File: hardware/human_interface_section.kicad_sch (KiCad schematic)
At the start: 8 parts, among them J1 Conn_01x08, J2 Micro_SD_Card, SW1 SW_Push, SW2 SW_Push, SW3 SW_Push, SW4 SW_Push, SW5 SW_Push, SW6 SW_Push

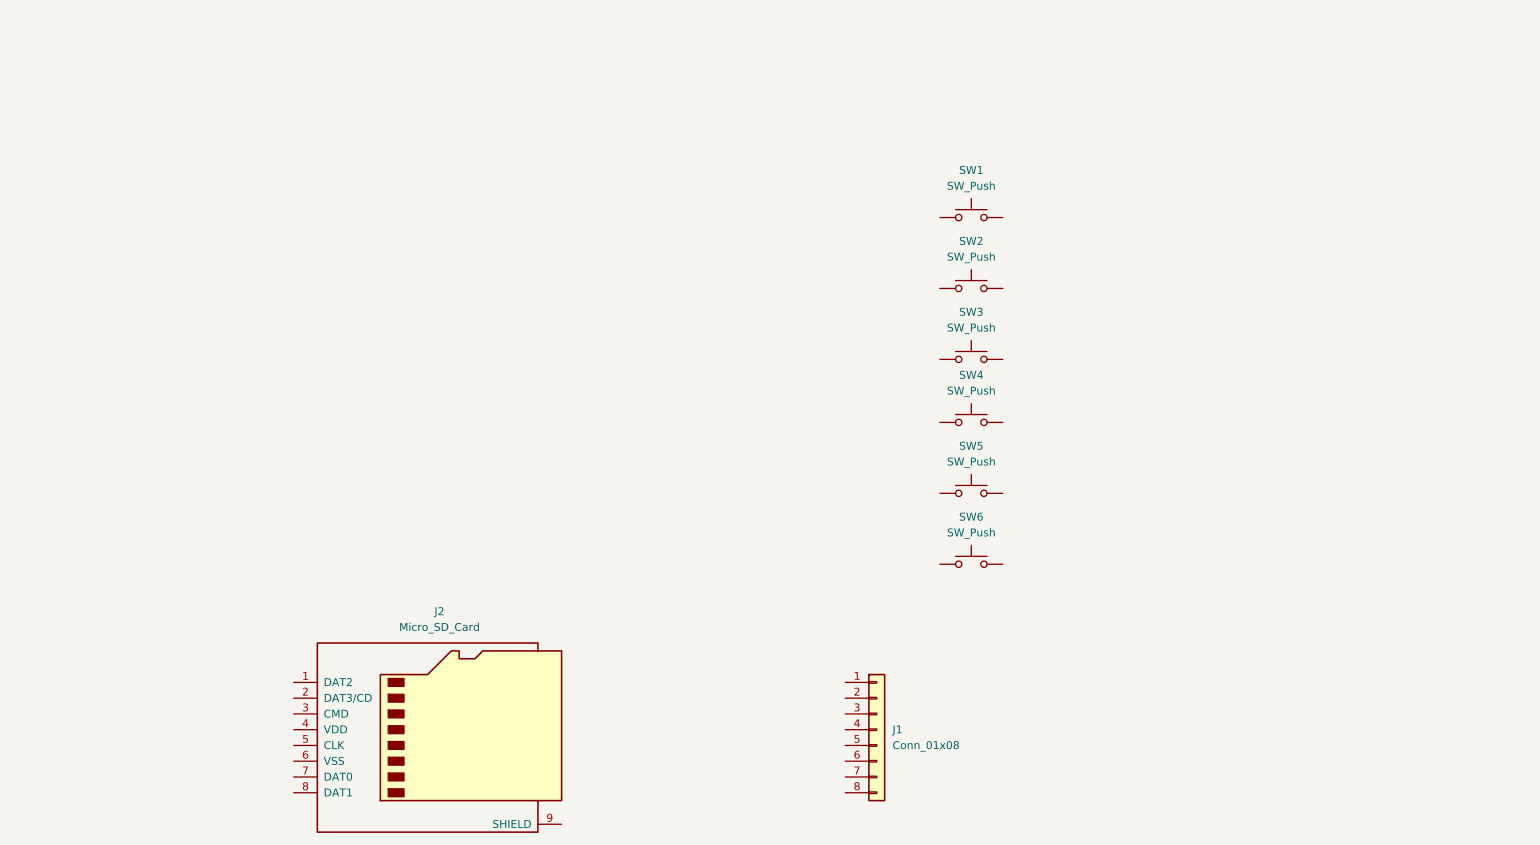
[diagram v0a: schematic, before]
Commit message: Human Interface section finished
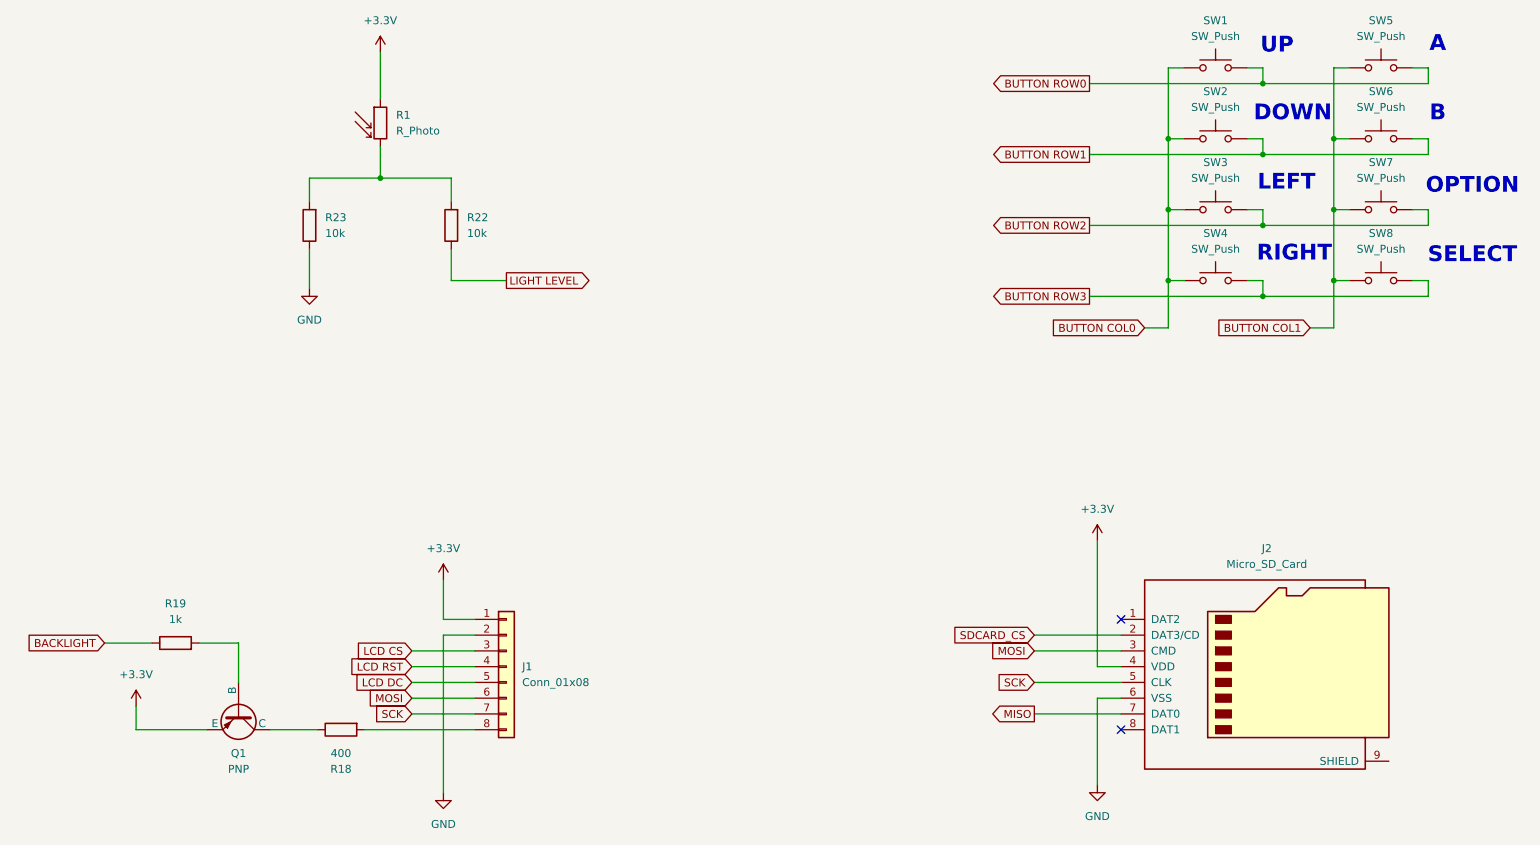
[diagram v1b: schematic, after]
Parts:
- added Q1: PNP, symbol Simulation_SPICE:PNP
- added R1: R_Photo, symbol Device:R_Photo
- added R18: 400, Resistor_SMD:R_0603_1608Metric, symbol Device:R
- added R19: 1k, Resistor_SMD:R_0603_1608Metric, symbol Device:R
- added R22, R23: 10k, Resistor_SMD:R_0603_1608Metric, symbol Device:R
- added SW7, SW8: SW_Push, symbol Switch:SW_Push
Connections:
- net BUTTON COL0: now reaches SW2.1
- net BUTTON COL0: now also SW1.1, SW3.1, SW4.1
- net BUTTON ROW1: now reaches SW2.2
- net BUTTON ROW1: now also SW6.2
- net BUTTON COL1: now reaches SW6.1
- net BUTTON COL1: now also SW5.1, SW7.1, SW8.1
- net BUTTON ROW2: now reaches SW3.2
- net BUTTON ROW2: now also SW7.2
- net BUTTON ROW0: now reaches SW1.2
- net BUTTON ROW0: now also SW5.2
- net BUTTON ROW3: now reaches SW4.2
- net BUTTON ROW3: now also SW8.2
- net SDCARD_CS: now reaches J2.2 (DAT3/CD)
- net MOSI: now reaches J2.3 (CMD)
- net MOSI: now also J1.6 (Pin_6)
- net +3.3V: now reaches J2.4 (VDD)
- net +3.3V: now also J1.1 (Pin_1), Q1.3 (E), R1.1
- net SCK: now reaches J2.5 (CLK)
- net SCK: now also J1.7 (Pin_7)
- net GND: now reaches J2.6 (VSS)
- net GND: now also J1.2 (Pin_2), R23.1
- net MISO: now reaches J2.7 (DAT0)
- net LCD CS: now reaches J1.3 (Pin_3)
- net LCD RST: now reaches J1.4 (Pin_4)
- net LCD DC: now reaches J1.5 (Pin_5)
- net at J1.8 (Pin_8): now also R18.2
- new net: Q1.2 (B), R19.2
- new net: R1.2, R22.2, R23.2
- new net: Q1.1 (C), R18.1
- new net BACKLIGHT: R19.1
- new net LIGHT LEVEL: R22.1
- no-connect marks 0 -> 2
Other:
- note added: "A"
- note added: "B"
- note added: "DOWN"
- note added: "LEFT"
- note added: "OPTION"
- note added: "RIGHT"
- note added: "SELECT"
- note added: "UP"
- moved on the sheet: J1, J2, SW1, SW2, SW3, SW4

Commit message: Moved MCU to general section
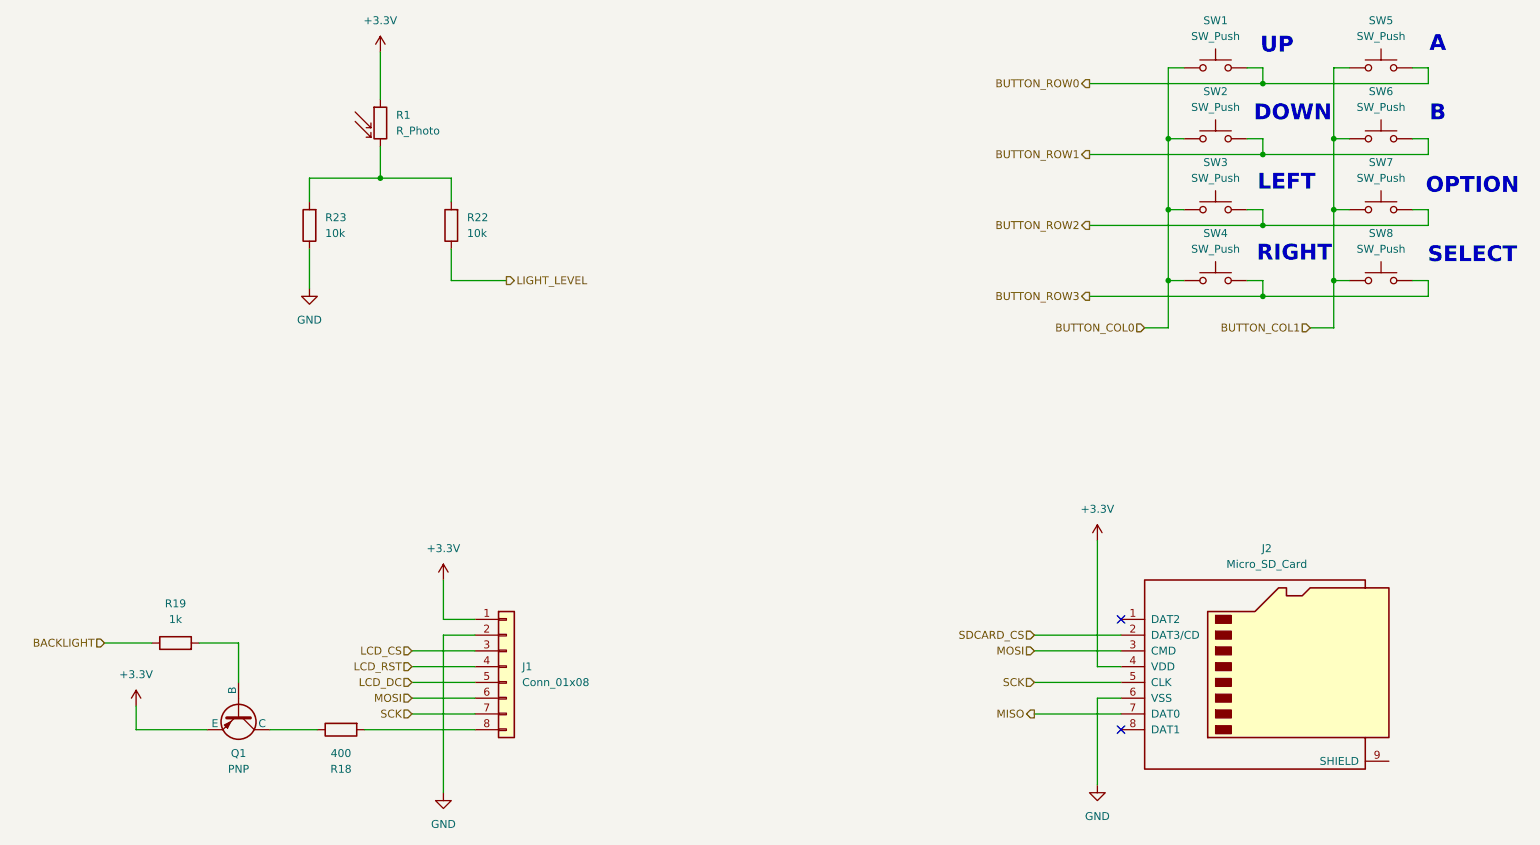
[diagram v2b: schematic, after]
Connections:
- net BUTTON COL0 renamed BUTTON_COL0
- net BUTTON COL1 renamed BUTTON_COL1
- net BUTTON ROW0 renamed BUTTON_ROW0
- net BUTTON ROW1 renamed BUTTON_ROW1
- net BUTTON ROW2 renamed BUTTON_ROW2
- net BUTTON ROW3 renamed BUTTON_ROW3
- net LCD CS renamed LCD_CS
- net LCD DC renamed LCD_DC
- net LCD RST renamed LCD_RST
- net LIGHT LEVEL renamed LIGHT_LEVEL
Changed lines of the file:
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@@
 		)
 	)
-	(global_label "BUTTON ROW3"
-		(shape output)
-		(at 194.31 73.66 180)
-		(fields_autoplaced yes)
+	(hierarchical_label "BACKLIGHT"
+		(shape input)
+		(at 35.56 129.54 180)
 		(effects
 			(font
@@
 			(justify right)
 		)
-		(property "Intersheetrefs" "${INTERSHEET_REFS}"
-			(at 177.8991 73.66 0)
-			(effects
-				(font
-					(size 1.27 1.27)
-				)
-				(justify right)
-				(hide yes)
-			)
-		)
 	)
-	(global_label "BUTTON ROW1"
-		(shape output)
-		(at 194.31 50.8 180)
-		(fields_autoplaced yes)
+	(hierarchical_label "LCD_DC"
+		(shape input)
+		(at 85.09 135.89 180)
 		(effects
 			(font
@@
 			(justify right)
 		)
-		(property "Intersheetrefs" "${INTERSHEET_REFS}"
-			(at 177.8991 50.8 0)
-			(effects
-				(font
-					(size 1.27 1.27)
-				)
-				(justify right)
-				(hide yes)
+	)
+	(hierarchical_label "LIGHT_LEVEL"
+		(shape output)
+		(at 100.33 71.12 0)
+		(effects
+			(font
+				(size 1.27 1.27)
 			)
+			(justify left)
 		)
 	)
-	(global_label "SCK"
-		(shape input)
-		(at 85.09 140.97 180)
-		(fields_autoplaced yes)
+	(hierarchical_label "BUTTON_ROW3"
+		(shape output)
+		(at 194.31 73.66 180)
 		(effects
 			(font
@@
 			(justify right)
 		)
-		(property "Intersheetrefs" "${INTERSHEET_REFS}"
-			(at 78.3553 140.97 0)
-			(effects
-				(font
-					(size 1.27 1.27)
-				)
-				(justify right)
-				(hide yes)
-			)
-		)
 	)
-	(global_label "BACKLIGHT"
+	(hierarchical_label "MOSI"
 		(shape input)
-		(at 35.56 129.54 180)
-		(fields_autoplaced yes)
+		(at 185.42 130.81 180)
 		(effects
 			(font
@@
 			(justify right)
 		)
-		(property "Intersheetrefs" "${INTERSHEET_REFS}"
-			(at 22.4752 129.54 0)
-			(effects
-				(font
-					(size 1.27 1.27)
-				)
-				(justify right)
-				(hide yes)
-			)
-		)
 	)
-	(global_label "SDCARD_CS"
+	(hierarchical_label "SDCARD_CS"
 		(shape input)
 		(at 185.42 128.27 180)
-		(fields_autoplaced yes)
 		(effects
 			(font
@@
 			(justify right)
 		)
-		(property "Intersheetrefs" "${INTERSHEET_REFS}"
-			(at 171.6096 128.27 0)
-			(effects
-				(font
-					(size 1.27 1.27)
-				)
-				(justify right)
-				(hide yes)
-			)
-		)
 	)
-	(global_label "MOSI"
+	(hierarchical_label "LCD_RST"
 		(shape input)
-		(at 185.42 130.81 180)
-		(fields_autoplaced yes)
+		(at 85.09 133.35 180)
 		(effects
 			(font
@@
 			(justify right)
 		)
-		(property "Intersheetrefs" "${INTERSHEET_REFS}"
-			(at 177.8386 130.81 0)
-			(effects
-				(font
-					(size 1.27 1.27)
-				)
-				(justify right)
-				(hide yes)
-			)
-		)
 	)
-	(global_label "BUTTON COL0"
+	(hierarchical_label "LCD_CS"
 		(shape input)
-		(at 203.2 78.74 180)
-		(fields_autoplaced yes)
+		(at 85.09 130.81 180)
 		(effects
 			(font
@@
 			(justify right)
 		)
-		(property "Intersheetrefs" "${INTERSHEET_REFS}"
-			(at 187.2124 78.74 0)
-			(effects
-				(font
-					(size 1.27 1.27)
-				)
-				(justify right)
-				(hide yes)
-			)
-		)
 	)
-	(global_label "LCD CS"
+	(hierarchical_label "MOSI"
 		(shape input)
-		(at 85.09 130.81 180)
-		(fields_autoplaced yes)
+		(at 85.09 138.43 180)
 		(effects
 			(font
@@
 			(justify right)
 		)
-		(property "Intersheetrefs" "${INTERSHEET_REFS}"
-			(at 75.0896 130.81 0)
-			(effects
-				(font
-					(size 1.27 1.27)
-				)
-				(justify right)
-				(hide yes)
-			)
-		)
 	)
-	(global_label "LIGHT LEVEL"
-		(shape output)
-		(at 100.33 71.12 0)
-		(fields_autoplaced yes)
-		(effects
-			(font
-				(size 1.27 1.27)
-			)
-			(justify left)
-		)
-		(property "Intersheetrefs" "${INTERSHEET_REFS}"
-			(at 114.9266 71.12 0)
-			(effects
-				(font
-					(size 1.27 1.27)
-				)
-				(justify left)
-				(hide yes)
-			)
-		)
-	)
-	(global_label "SCK"
+	(hierarchical_label "BUTTON_COL1"
 		(shape input)
-		(at 185.42 135.89 180)
-		(fields_autoplaced yes)
+		(at 229.87 78.74 180)
 		(effects
 			(font
@@
 			(justify right)
 		)
-		(property "Intersheetrefs" "${INTERSHEET_REFS}"
-			(at 178.6853 135.89 0)
-			(effects
-				(font
-					(size 1.27 1.27)
-				)
-				(justify right)
-				(hide yes)
-			)
-		)
 	)
-	(global_label "BUTTON ROW2"
-		(shape output)
-		(at 194.31 62.23 180)
-		(fields_autoplaced yes)
+	(hierarchical_label "SCK"
+		(shape input)
+		(at 85.09 140.97 180)
 		(effects
 			(font
@@
 			(justify right)
 		)
-		(property "Intersheetrefs" "${INTERSHEET_REFS}"
-			(at 177.8991 62.23 0)
-			(effects
-				(font
-					(size 1.27 1.27)
-				)
-				(justify right)
-				(hide yes)
-			)
-		)
 	)
-	(global_label "BUTTON COL1"
+	(hierarchical_label "BUTTON_COL0"
 		(shape input)
-		(at 229.87 78.74 180)
-		(fields_autoplaced yes)
+		(at 203.2 78.74 180)
 		(effects
 			(font
@@
 			(justify right)
 		)
-		(property "Intersheetrefs" "${INTERSHEET_REFS}"
-			(at 213.8824 78.74 0)
-			(effects
-				(font
-					(size 1.27 1.27)
-				)
-				(justify right)
-				(hide yes)
-			)
-		)
 	)
-	(global_label "BUTTON ROW0"
-		(shape output)
-		(at 194.31 39.37 180)
-		(fields_autoplaced yes)
+	(hierarchical_label "SCK"
+		(shape input)
+		(at 185.42 135.89 180)
 		(effects
 			(font
@@
 			(justify right)
 		)
-		(property "Intersheetrefs" "${INTERSHEET_REFS}"
-			(at 177.8991 39.37 0)
-			(effects
-				(font
-					(size 1.27 1.27)
-				)
-				(justify right)
-				(hide yes)
-			)
-		)
 	)
-	(global_label "MOSI"
-		(shape input)
-		(at 85.09 138.43 180)
-		(fields_autoplaced yes)
+	(hierarchical_label "BUTTON_ROW0"
+		(shape output)
+		(at 194.31 39.37 180)
 		(effects
 			(font
@@
 			(justify right)
 		)
-		(property "Intersheetrefs" "${INTERSHEET_REFS}"
-			(at 77.5086 138.43 0)
-			(effects
-				(font
-					(size 1.27 1.27)
-				)
-				(justify right)
-				(hide yes)
-			)
-		)
 	)
-	(global_label "MISO"
+	(hierarchical_label "BUTTON_ROW2"
 		(shape output)
-		(at 185.42 140.97 180)
-		(fields_autoplaced yes)
+		(at 194.31 62.23 180)
 		(effects
 			(font
@@
 			(justify right)
 		)
-		(property "Intersheetrefs" "${INTERSHEET_REFS}"
-			(at 177.8386 140.97 0)
-			(effects
-				(font
-					(size 1.27 1.27)
-				)
-				(justify right)
-				(hide yes)
-			)
-		)
 	)
-	(global_label "LCD DC"
-		(shape input)
-		(at 85.09 135.89 180)
-		(fields_autoplaced yes)
+	(hierarchical_label "MISO"
+		(shape output)
+		(at 185.42 140.97 180)
 		(effects
 			(font
@@
 			(justify right)
 		)
-		(property "Intersheetrefs" "${INTERSHEET_REFS}"
-			(at 75.0291 135.89 0)
-			(effects
-				(font
-					(size 1.27 1.27)
-				)
-				(justify right)
-				(hide yes)
-			)
-		)
 	)
-	(global_label "LCD RST"
-		(shape input)
-		(at 85.09 133.35 180)
-		(fields_autoplaced yes)
+	(hierarchical_label "BUTTON_ROW1"
+		(shape output)
+		(at 194.31 50.8 180)
 		(effects
 			(font
@@
 			(justify right)
 		)
-		(property "Intersheetrefs" "${INTERSHEET_REFS}"
-			(at 74.122 133.35 0)
-			(effects
-				(font
-					(size 1.27 1.27)
-				)
-				(justify right)
-				(hide yes)
-			)
-		)
 	)
